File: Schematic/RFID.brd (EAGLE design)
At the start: 160 x 100 mm, 6 parts, among them U1 HTRC11001T/02EE,11

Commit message: IC Connections, STM32 Pins
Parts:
- added C1, C2: 5pF, rcl:C0805
- added C3: (no value), rcl:C0805
- added C4: 10uF, rcl:C0805
- added C5, C6, C7: 100nF, rcl:C0805
- added IC1: B82450A1084C000, B82450A1084C000:B82450A_(11.4_X_3.5)
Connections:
- removed net VSS: U1.1
- new net 5V_USB_CHG: JP5.4
- new net AGND: JP5.16
- new net ANT1: IC1.1
- new net ANT2: C3.2, IC1.2
- new net AVDD: JP4.4
- new net N$6: C1.1, U1.6
- new net N$7: C2.1, U1.7
- new net N$8: C6.1, U1.12
- new net N$9: C7.1, U1.13
- new net PA10: JP4.17
- new net PA11: JP5.7
- new net PA12: JP5.6
- new net PA5: JP4.6, U1.8
- new net PA6: JP4.7, U1.10
- new net PA7: JP4.8, U1.9
- new net PA8: JP4.12
- new net PA9: JP4.11
- new net PB1: JP5.12
- new net PB10: JP4.13
- new net PB11: JP5.9
- new net PB12: JP5.8
- new net PB13: JP5.15
- new net PB14: JP5.14
- new net PB15: JP5.13
- new net PB2: JP5.11
- new net PB3: JP4.16
- new net PB4: JP4.14
- new net PB5: JP4.15
- new net PB6: JP4.9
- new net PB8: JP4.2
- new net PB9: JP4.3
- new net PC4: JP5.17
- new net PC4/PA2: JP4.18
- new net PC5: JP5.3
- new net PC5/PA3: JP4.19
- new net PC6: JP5.2
- new net PC7: JP4.10
- new net PC8: JP5.1
- new net PC9: JP4.1
- new net RX: U1.14
- new net TX1: U1.4
- new net TX2: C3.1, U1.2
- net 5V: now also C4.1, C5.1
- net GND: now also C1.2, C2.2, C4.2, C5.2, C6.2, C7.2, JP4.5, JP5.10, U1.1, U1.5
- net NC: now also JP4.20, JP5.18, JP5.19, JP5.20, JP5.5

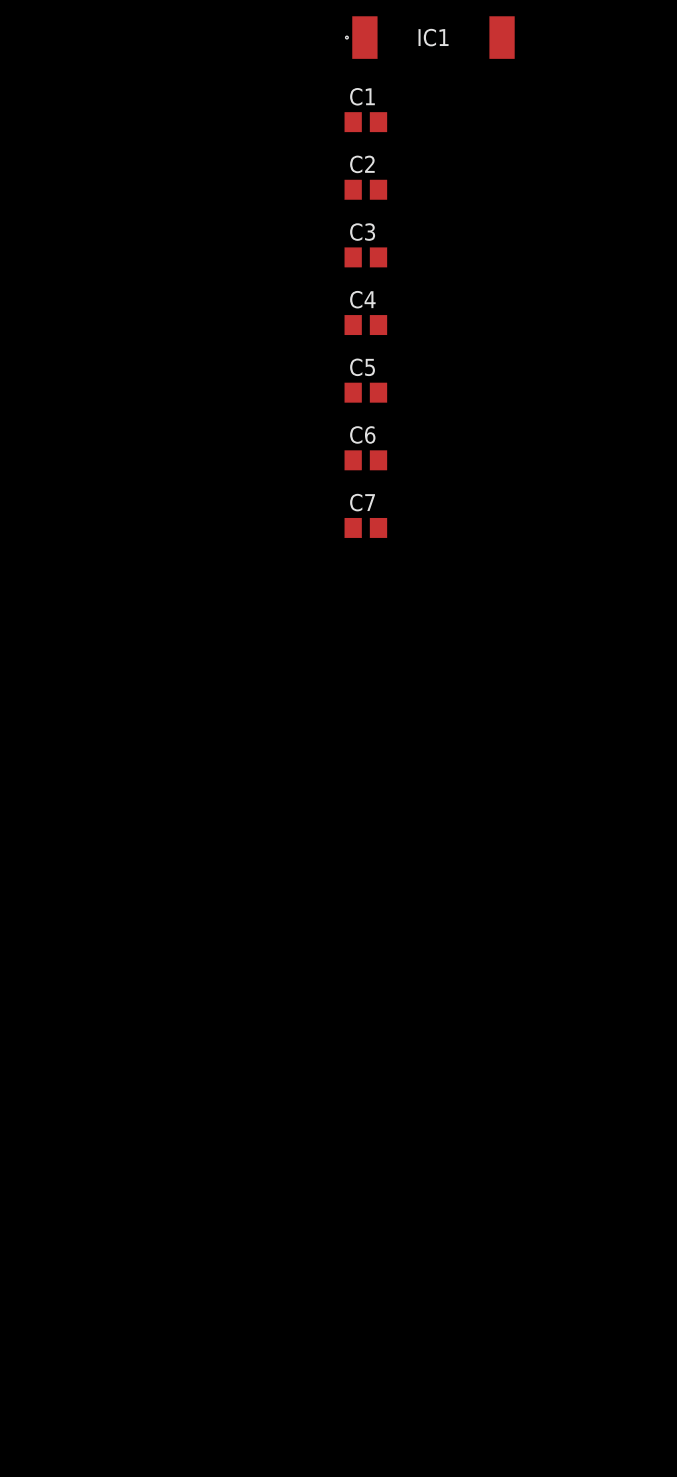
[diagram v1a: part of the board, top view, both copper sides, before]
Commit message: Schematic without impedance matching
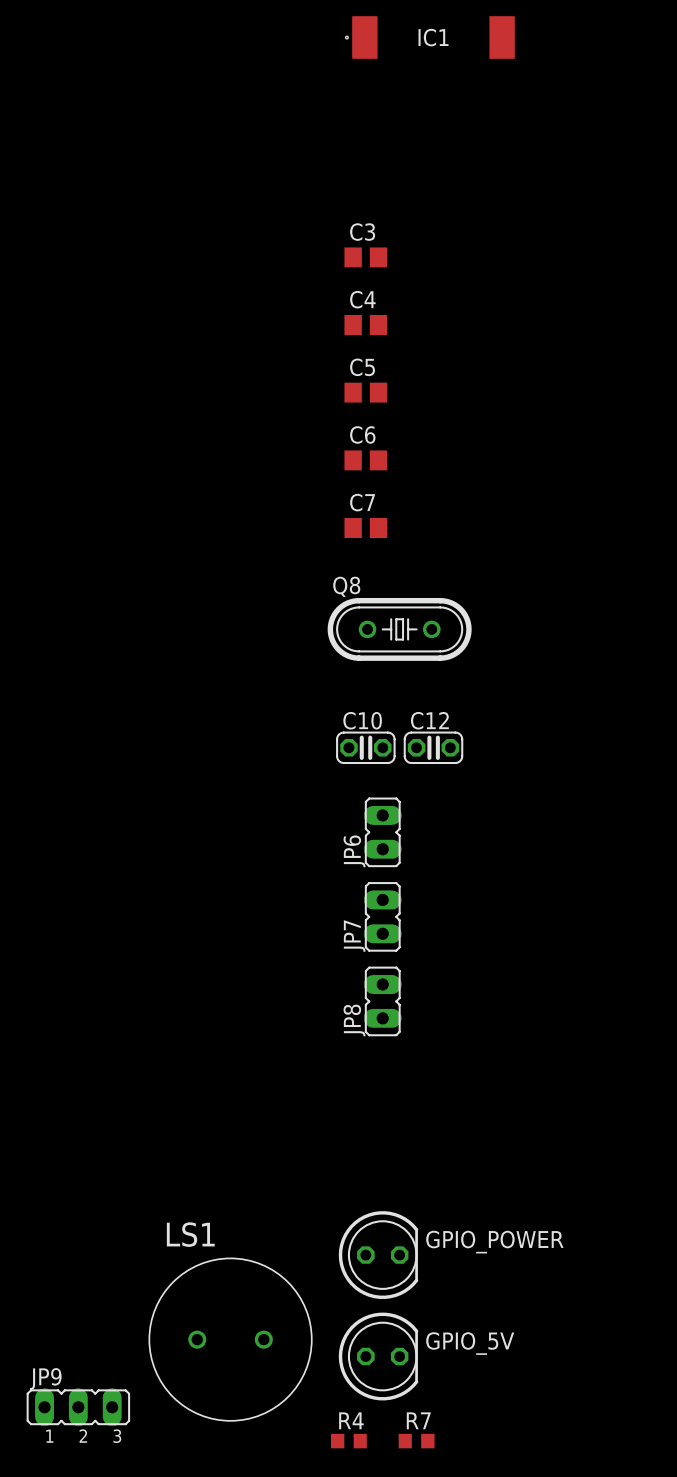
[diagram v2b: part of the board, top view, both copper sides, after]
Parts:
- removed C1, C2: 5pF, rcl:C0805
- added C10, C12: 5pF, resistor:C025-024X044
- added GPIO_5V, GPIO_POWER: 16V, led:LED5MM
- added JP6, JP7, JP8: (no value), jumper:JP1
- added JP9: (no value), jumper:JP2
- added LS1: PS1240P02BT, PS1240P02BT:XDCR_PS1240P02BT
- added Q8: 125kHz, crystal:HC49/S
- added R4, R7: 0.2k, adafruit:R0603
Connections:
- net PA5 renamed SCLK
- removed net N$6: C1.1, U1.6
- removed net N$7: C2.1, U1.7
- removed net NC: JP1.13, JP1.20, JP1.5, JP2.20, JP2.5, JP2.6, JP4.20, JP5.18, JP5.19, JP5.20, JP5.5
- removed net PA6: JP4.7, U1.10
- removed net PA7: JP4.8, U1.9
- removed net PC_10: JP2.1
- removed net PC_2: JP2.18
- removed net PC_3: JP2.19
- new net CRY_N: C12.1, Q8.2, U1.7
- new net CRY_P: C10.1, Q8.1, U1.6
- new net ENTRY: JP2.18, R7.2
- new net IN: JP2.1, JP9.1
- new net N$2: GPIO_POWER.A, R4.2
- new net N$3: GPIO_5V.A, R7.1
- new net SPI_DIN: JP4.8, JP8.1, U1.9
- new net SPI_DOUT: JP4.7, JP8.2, U1.10
- new net ~ENTRY: JP2.19, LS1.2, R4.1
- net 3V3: now also JP7.1
- net 5V: now also JP6.1, JP9.2
- net GND: now also C10.2, C12.2, GPIO_5V.K, GPIO_POWER.K, JP6.2, JP7.2, JP9.3, LS1.1; no longer C1.2, C2.2

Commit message: Buzzer+impedance matching ckt incorporated
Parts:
- added C1: (no value), rcl:C0805
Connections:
- net PWM2/1: now also LS1.2
- net TX1: now also C1.2
- net TX2: now also C1.1
- net ~ENTRY: no longer LS1.2
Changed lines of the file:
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@@
 <attribute name="VALUE" x="-67.056" y="-141.478" size="1.27" layer="27" ratio="10"/>
+</element>
+<element name="C1" library="rcl" library_urn="urn:adsk.eagle:library:334" package="C0805" package3d_urn="urn:adsk.eagle:package:23617/2" value="" x="-64.77" y="-146.05" smashed="yes">
+<attribute name="NAME" x="-66.04" y="-144.78" size="1.27" layer="25"/>
+<attribute name="POPULARITY" value="63" x="-64.77" y="-146.05" size="1.778" layer="27" display="off"/>
+<attribute name="SPICEPREFIX" value="C" x="-64.77" y="-146.05" size="1.778" layer="27" display="off"/>
+<attribute name="VALUE" x="-66.04" y="-148.59" size="1.27" layer="27"/>
 </element>
 </elements>
@@
 <contactref element="JP2" pad="9"/>
 <contactref element="JP1" pad="14"/>
+<contactref element="LS1" pad="2"/>
+<wire x1="-21.59" y1="-10.16" x2="-49.57" y2="-132.08" width="0" layer="19" extent="1-1"/>
 <wire x1="-8.89" y1="-3.81" x2="-21.59" y2="-10.16" width="0" layer="19" extent="1-1"/>
 </signal>
@@
 <contactref element="U1" pad="2"/>
 <contactref element="C3" pad="1"/>
+<contactref element="C1" pad="1"/>
+<wire x1="-42.86" y1="-50.8" x2="-65.72" y2="-146.05" width="0" layer="19" extent="1-1"/>
 <wire x1="-43.2308" y1="11.43" x2="-42.86" y2="-50.8" width="0" layer="19" extent="1-1"/>
 </signal>
 <signal name="TX1">
 <contactref element="U1" pad="4"/>
+<contactref element="C1" pad="2"/>
+<wire x1="-43.2308" y1="8.89" x2="-63.82" y2="-146.05" width="0" layer="19" extent="1-1"/>
 </signal>
 <signal name="RX">
@@
 </signal>
 <signal name="~ENTRY" class="2">
-<contactref element="LS1" pad="2"/>
 <contactref element="R4" pad="1"/>
 <contactref element="JP2" pad="19"/>
-<wire x1="-49.57" y1="-132.08" x2="-44.03" y2="-139.7" width="0" layer="19" extent="1-1"/>
-<wire x1="3.81" y1="-10.16" x2="-49.57" y2="-132.08" width="0" layer="19" extent="1-1"/>
+<wire x1="3.81" y1="-10.16" x2="-44.03" y2="-139.7" width="0" layer="19" extent="1-1"/>
 </signal>
 <signal name="IN">

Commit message: Schematic v1
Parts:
- removed JP3: (no value), adafruit:1X20
- added R1, R3, R5: (no value), adafruit:R0603
- added R2, R6, R9: 0ohm, adafruit:R0603
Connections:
- new net ANT3: C1.1, C3.1, R2.2
- new net ENTRY1: R3.2
- new net N$4: R1.1, R6.2
- net ANT1: now also R5.2
- net ANT2: now also R1.2
- net RX: now also R6.1
- net TX1: now also R3.1, R5.1, R9.1, R9.2
- net TX2: now also R2.1; no longer C1.1, C3.1
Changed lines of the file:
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@@
 <attribute name="VALUE" x="-43.18" y="-13.335" size="1.27" layer="27"/>
-</element>
-<element name="JP3" library="adafruit" package="1X20" value="" x="-17.78" y="-16.51" smashed="yes">
-<attribute name="NAME" x="-43.2562" y="-14.6812" size="1.27" layer="25" ratio="10"/>
-<attribute name="VALUE" x="-43.18" y="-19.685" size="1.27" layer="27"/>
 </element>
 <element name="JP4" library="adafruit" package="1X20" value="" x="-17.78" y="-22.86" smashed="yes">
@@
 <attribute name="SPICEPREFIX" value="C" x="-64.77" y="-146.05" size="1.778" layer="27" display="off"/>
 <attribute name="VALUE" x="-66.04" y="-148.59" size="1.27" layer="27"/>
+</element>
+<element name="R9" library="adafruit" package="R0603" value="0ohm" x="-66.04" y="-149.86" smashed="yes">
+<attribute name="NAME" x="-66.929" y="-148.971" size="1.27" layer="25"/>
+<attribute name="VALUE" x="-66.929" y="-151.892" size="1.27" layer="27"/>
+</element>
+<element name="R2" library="adafruit" package="R0603" value="0ohm" x="-66.04" y="-156.21" smashed="yes">
+<attribute name="NAME" x="-66.929" y="-155.321" size="1.27" layer="25"/>
+<attribute name="VALUE" x="-66.929" y="-158.242" size="1.27" layer="27"/>
+</element>
+<element name="R6" library="adafruit" package="R0603" value="0ohm" x="-66.04" y="-162.56" smashed="yes">
+<attribute name="NAME" x="-66.929" y="-161.671" size="1.27" layer="25"/>
+<attribute name="VALUE" x="-66.929" y="-164.592" size="1.27" layer="27"/>
+</element>
+<element name="R1" library="adafruit" package="R0603" value="" x="-66.04" y="-168.91" smashed="yes">
+<attribute name="NAME" x="-66.929" y="-168.021" size="1.27" layer="25"/>
+<attribute name="VALUE" x="-66.929" y="-170.942" size="1.27" layer="27"/>
+</element>
+<element name="R3" library="adafruit" package="R0603" value="" x="-66.04" y="-175.26" smashed="yes">
+<attribute name="NAME" x="-66.929" y="-174.371" size="1.27" layer="25"/>
+<attribute name="VALUE" x="-66.929" y="-177.292" size="1.27" layer="27"/>
+</element>
+<element name="R5" library="adafruit" package="R0603" value="" x="-66.04" y="-181.61" smashed="yes">
+<attribute name="NAME" x="-66.929" y="-180.721" size="1.27" layer="25"/>
+<attribute name="VALUE" x="-66.929" y="-183.642" size="1.27" layer="27"/>
 </element>
 </elements>
@@
 <signal name="ANT1">
 <contactref element="IC1" pad="1"/>
+<contactref element="R5" pad="2"/>
+<wire x1="-41.98" y1="-34.29" x2="-65.19" y2="-181.61" width="0" layer="19" extent="1-1"/>
 </signal>
 <signal name="ANT2">
 <contactref element="IC1" pad="2"/>
 <contactref element="C3" pad="2"/>
+<contactref element="R1" pad="2"/>
+<wire x1="-40.96" y1="-50.8" x2="-65.19" y2="-168.91" width="0" layer="19" extent="1-1"/>
 <wire x1="-31.68" y1="-34.29" x2="-40.96" y2="-50.8" width="0" layer="19" extent="1-1"/>
 </signal>
@@
 <signal name="TX2">
 <contactref element="U1" pad="2"/>
-<contactref element="C3" pad="1"/>
-<contactref element="C1" pad="1"/>
-<wire x1="-42.86" y1="-50.8" x2="-65.72" y2="-146.05" width="0" layer="19" extent="1-1"/>
-<wire x1="-43.2308" y1="11.43" x2="-42.86" y2="-50.8" width="0" layer="19" extent="1-1"/>
+<contactref element="R2" pad="1"/>
+<wire x1="-43.2308" y1="11.43" x2="-66.89" y2="-156.21" width="0" layer="19" extent="1-1"/>
 </signal>
 <signal name="TX1">
 <contactref element="U1" pad="4"/>
 <contactref element="C1" pad="2"/>
+<contactref element="R9" pad="2"/>
+<contactref element="R9" pad="1"/>
+<contactref element="R3" pad="1"/>
+<contactref element="R5" pad="1"/>
+<wire x1="-66.89" y1="-175.26" x2="-66.89" y2="-181.61" width="0" layer="19" extent="1-1"/>
+<wire x1="-66.89" y1="-149.86" x2="-66.89" y2="-175.26" width="0" layer="19" extent="1-1"/>
+<wire x1="-65.19" y1="-149.86" x2="-66.89" y2="-149.86" width="0" layer="19" extent="1-1"/>
+<wire x1="-63.82" y1="-146.05" x2="-65.19" y2="-149.86" width="0" layer="19" extent="1-1"/>
 <wire x1="-43.2308" y1="8.89" x2="-63.82" y2="-146.05" width="0" layer="19" extent="1-1"/>
 </signal>
 <signal name="RX">
 <contactref element="U1" pad="14"/>
+<contactref element="R6" pad="1"/>
+<wire x1="-38.0492" y1="12.7" x2="-66.89" y2="-162.56" width="0" layer="19" extent="1-1"/>
 </signal>
 <signal name="N$8">
@@
 <wire x1="-41.91" y1="-10.16" x2="-66.04" y2="-137.16" width="0" layer="19" extent="1-1"/>
 </signal>
+<signal name="ANT3">
+<contactref element="C3" pad="1"/>
+<contactref element="C1" pad="1"/>
+<contactref element="R2" pad="2"/>
+<wire x1="-65.72" y1="-146.05" x2="-65.19" y2="-156.21" width="0" layer="19" extent="1-1"/>
+<wire x1="-42.86" y1="-50.8" x2="-65.72" y2="-146.05" width="0" layer="19" extent="1-1"/>
+</signal>
+<signal name="N$4">
+<contactref element="R6" pad="2"/>
+<contactref element="R1" pad="1"/>
+<wire x1="-65.19" y1="-162.56" x2="-66.89" y2="-168.91" width="0" layer="19" extent="1-1"/>
+</signal>
+<signal name="ENTRY1">
+<contactref element="R3" pad="2"/>
+</signal>
 </signals>

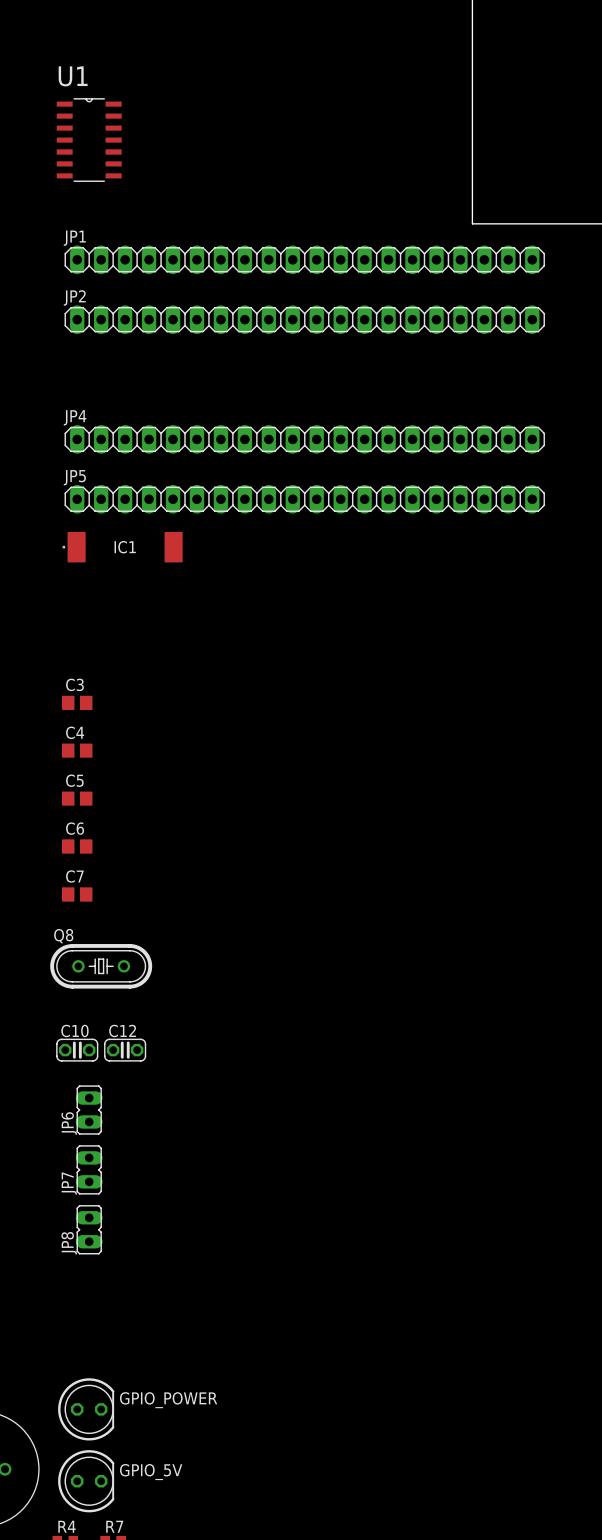
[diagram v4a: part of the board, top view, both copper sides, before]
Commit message: Placed board iter1
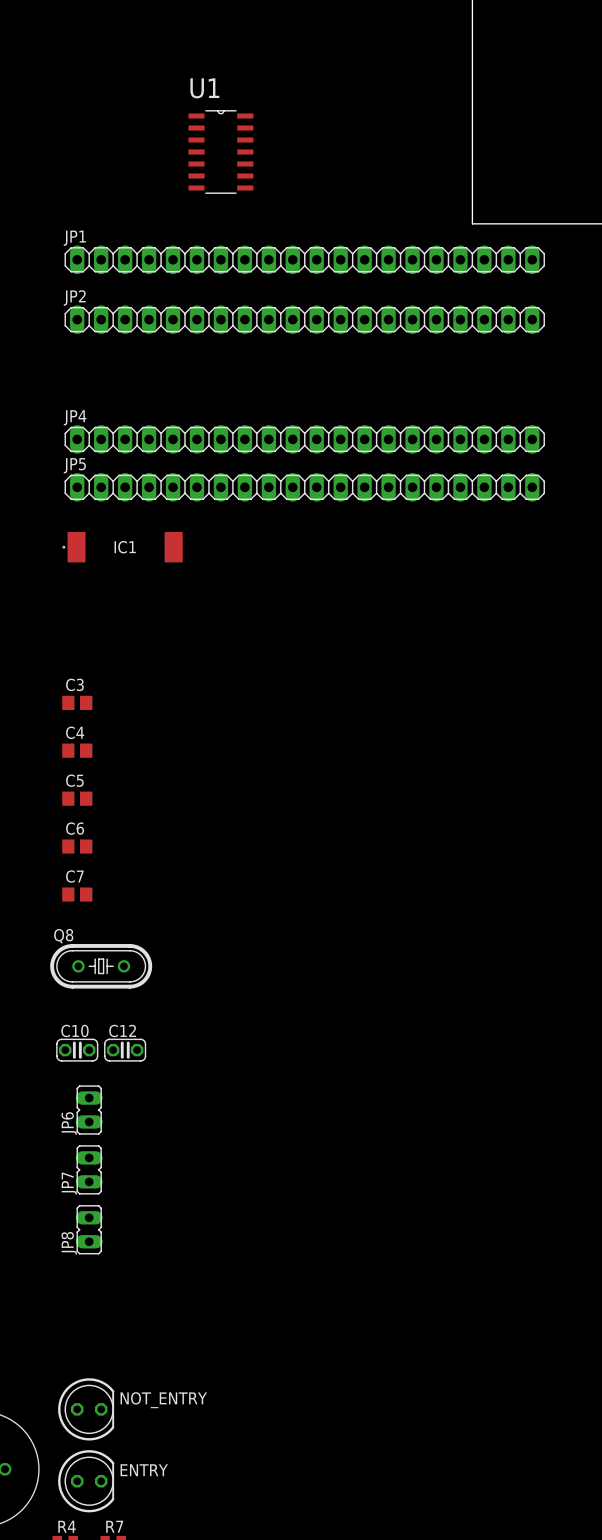
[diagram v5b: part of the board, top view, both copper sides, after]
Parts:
- moved U1 14.0 mm to (-26.7, 7.62)
- moved JP5 1.27 mm to (-17.8, -27.9)
- renumbered GPIO_5V to ENTRY, GPIO_POWER to NOT_ENTRY
